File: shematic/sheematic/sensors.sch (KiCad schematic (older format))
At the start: 7 parts

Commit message: cpu updated
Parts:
- IC1: renamed from IC?; symbol bmp180:BMP180 -> sheematic-rescue:BMP180-bmp180
- gave numbers to parts that had none: 6
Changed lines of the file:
@@
 $EndDescr
 $Comp
-L Sensor_Pressure:BMP280 U?
+L Sensor_Pressure:BMP280 U2
 U 1 1 60297DD8
 P 3800 2000
-F 0 "U?" H 4030 2096 50  0000 L CNN
+F 0 "U2" H 4030 2096 50  0000 L CNN
 F 1 "BMP280" H 4030 2005 50  0000 L CNN
 F 2 "Package_LGA:Bosch_LGA-8_2x2.5mm_P0.65mm_ClockwisePinNumbering" H 3800 1300 50  0001 C CNN
@@
 $EndComp
 $Comp
-L Sensor_Gas:CCS811 U?
+L Sensor_Gas:CCS811 U3
 U 1 1 60298425
 P 3800 3900
-F 0 "U?" H 3800 4581 50  0000 C CNN
+F 0 "U3" H 3800 4581 50  0000 C CNN
 F 1 "CCS811" H 3800 4490 50  0000 C CNN
 F 2 "Package_LGA:AMS_LGA-10-1EP_2.7x4mm_P0.6mm" H 3800 3300 50  0001 C CNN
@@
 $EndComp
 $Comp
-L Sensor_Humidity:Si7020-A20 U?
+L Sensor_Humidity:Si7020-A20 U4
 U 1 1 60299163
 P 7000 1900
-F 0 "U?" H 7444 1946 50  0000 L CNN
+F 0 "U4" H 7444 1946 50  0000 L CNN
 F 1 "Si7020-A20" H 7444 1855 50  0000 L CNN
 F 2 "Package_DFN_QFN:DFN-6-1EP_3x3mm_P1mm_EP1.5x2.4mm" H 7000 1500 50  0001 C CNN
@@
 $EndComp
 $Comp
-L Sensor_Humidity:ENS210 U?
+L Sensor_Humidity:ENS210 U5
 U 1 1 602998ED
 P 9050 1900
-F 0 "U?" H 9280 1946 50  0000 L CNN
+F 0 "U5" H 9280 1946 50  0000 L CNN
 F 1 "ENS210" H 9280 1855 50  0000 L CNN
 F 2 "Package_DFN_QFN:AMS_QFN-4-1EP_2x2mm_P0.95mm_EP0.7x1.6mm" H 9050 1500 50  0001 C CNN
@@
 $EndComp
 $Comp
-L bmp180:BMP180 IC?
+L sheematic-rescue:BMP180-bmp180 IC?
 U 1 1 60297945
 P 1300 1850
-F 0 "IC?" H 1850 2115 50  0000 C CNN
+AR Path="/60297945" Ref="IC?"  Part="1"
+AR Path="/60296418/60297945" Ref="IC1"  Part="1"
+F 0 "IC1" H 1850 2115 50  0000 C CNN
 F 1 "BMP180" H 1850 2024 50  0000 C CNN
 F 2 "BMP180" H 2250 1950 50  0001 L CNN
@@
 $EndComp
 $Comp
-L power:GND #PWR?
+L power:GND #PWR0101
 U 1 1 6029BE6D
 P 2400 2650
-F 0 "#PWR?" H 2400 2400 50  0001 C CNN
+F 0 "#PWR0101" H 2400 2400 50  0001 C CNN
 F 1 "GND" H 2405 2477 50  0000 C CNN
 F 2 "" H 2400 2650 50  0001 C CNN
@@
 $EndComp
 $Comp
-L power:GND #PWR?
+L power:GND #PWR0102
 U 1 1 6029C3A8
 P 3800 2650
-F 0 "#PWR?" H 3800 2400 50  0001 C CNN
+F 0 "#PWR0102" H 3800 2400 50  0001 C CNN
 F 1 "GND" H 3805 2477 50  0000 C CNN
 F 2 "" H 3800 2650 50  0001 C CNN
@@
 $EndComp
 $Comp
-L power:GND #PWR?
+L power:GND #PWR0103
 U 1 1 6029C50E
 P 3900 2650
-F 0 "#PWR?" H 3900 2400 50  0001 C CNN
+F 0 "#PWR0103" H 3900 2400 50  0001 C CNN
 F 1 "GND" H 3905 2477 50  0000 C CNN
 F 2 "" H 3900 2650 50  0001 C CNN
@@
 $EndComp
 $Comp
-L power:GND #PWR?
+L power:GND #PWR0104
 U 1 1 6029C6CB
 P 3800 4600
-F 0 "#PWR?" H 3800 4350 50  0001 C CNN
+F 0 "#PWR0104" H 3800 4350 50  0001 C CNN
 F 1 "GND" H 3805 4427 50  0000 C CNN
 F 2 "" H 3800 4600 50  0001 C CNN
@@
 $EndComp
 $Comp
-L power:GND #PWR?
+L power:GND #PWR0105
 U 1 1 6029CA3B
 P 7750 2650
-F 0 "#PWR?" H 7750 2400 50  0001 C CNN
+F 0 "#PWR0105" H 7750 2400 50  0001 C CNN
 F 1 "GND" H 7755 2477 50  0000 C CNN
 F 2 "" H 7750 2650 50  0001 C CNN
@@
 	1100 2050 1300 2050
 $Comp
-L power:+3.3V #PWR?
+L power:+3.3V #PWR0106
 U 1 1 6029E802
 P 1050 1500
-F 0 "#PWR?" H 1050 1350 50  0001 C CNN
+F 0 "#PWR0106" H 1050 1350 50  0001 C CNN
 F 1 "+3.3V" H 1065 1673 50  0000 C CNN
 F 2 "" H 1050 1500 50  0001 C CNN
@@
 Connection ~ 1100 1950
 $Comp
-L power:+3.3V #PWR?
+L power:+3.3V #PWR0107
 U 1 1 6029EF9E
 P 3800 1300
-F 0 "#PWR?" H 3800 1150 50  0001 C CNN
+F 0 "#PWR0107" H 3800 1150 50  0001 C CNN
 F 1 "+3.3V" H 3815 1473 50  0000 C CNN
 F 2 "" H 3800 1300 50  0001 C CNN
@@
 	9150 1200 9150 1600
 $Comp
-L power:+3.3V #PWR?
+L power:+3.3V #PWR0108
 U 1 1 602A1788
 P 8550 1050
-F 0 "#PWR?" H 8550 900 50  0001 C CNN
+F 0 "#PWR0108" H 8550 900 50  0001 C CNN
 F 1 "+3.3V" H 8565 1223 50  0000 C CNN
 F 2 "" H 8550 1050 50  0001 C CNN
@@
 SDA
 $Comp
-L Device:R R?
+L Device:R R1
 U 1 1 602A736D
 P 5250 1150
-F 0 "R?" H 5320 1196 50  0000 L CNN
+F 0 "R1" H 5320 1196 50  0000 L CNN
 F 1 "R" H 5320 1105 50  0000 L CNN
 F 2 "" V 5180 1150 50  0001 C CNN
@@
 $EndComp
 $Comp
-L Device:R R?
+L Device:R R2
 U 1 1 602A7929
 P 5550 1150
-F 0 "R?" H 5620 1196 50  0000 L CNN
+F 0 "R2" H 5620 1196 50  0000 L CNN
 F 1 "R" H 5620 1105 50  0000 L CNN
 F 2 "" V 5480 1150 50  0001 C CNN
@@
 SDA
 $Comp
-L power:+3.3V #PWR?
+L power:+3.3V #PWR0109
 U 1 1 602A8243
 P 5250 800
-F 0 "#PWR?" H 5250 650 50  0001 C CNN
+F 0 "#PWR0109" H 5250 650 50  0001 C CNN
 F 1 "+3.3V" H 5265 973 50  0000 C CNN
 F 2 "" H 5250 800 50  0001 C CNN
@@
 $EndComp
 $Comp
-L power:+3.3V #PWR?
+L power:+3.3V #PWR0110
 U 1 1 602A872F
 P 5550 800
-F 0 "#PWR?" H 5550 650 50  0001 C CNN
+F 0 "#PWR0110" H 5550 650 50  0001 C CNN
 F 1 "+3.3V" H 5565 973 50  0000 C CNN
 F 2 "" H 5550 800 50  0001 C CNN

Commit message: updated
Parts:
- removed IC1: BMP180, BMP180, symbol sheematic-rescue:BMP180-bmp180
- added IC1: BMP180, Sensor:BMP180, symbol SamacSys_Parts:BMP180
- added R3, R4, R5, R6, R7: R, symbol Device:R
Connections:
- net +3V3: now also U3.6 (VDD), IC1.2 (VDD), IC1.3 (VDDIO), R3.1, R5.1, R6.1, R7.1
- net GND: now also U3.11 (GND), IC1.7 (GND), R4.1
- net SCL: now also U3.10 (SCL), IC1.5 (SCL)
- net SDA: now also U3.9 (SDA), IC1.6 (SDA)
- net at U3.1 (ADDR): now also R3.2, R4.2
- net CCS811_nRESET: now reaches U3.2 (~RESET)
- net CCS811_nRESET: now also R6.2
- net CCS811_nINT: now reaches U3.3 (~INT)
- net CCS811_nINT: now also R5.2
- net at U3.4 (PWM): now also U3.5 (Sense)
- net CCS811_nWAKE: now reaches U3.7 (~WAKE)
- net CCS811_nWAKE: now also R7.2

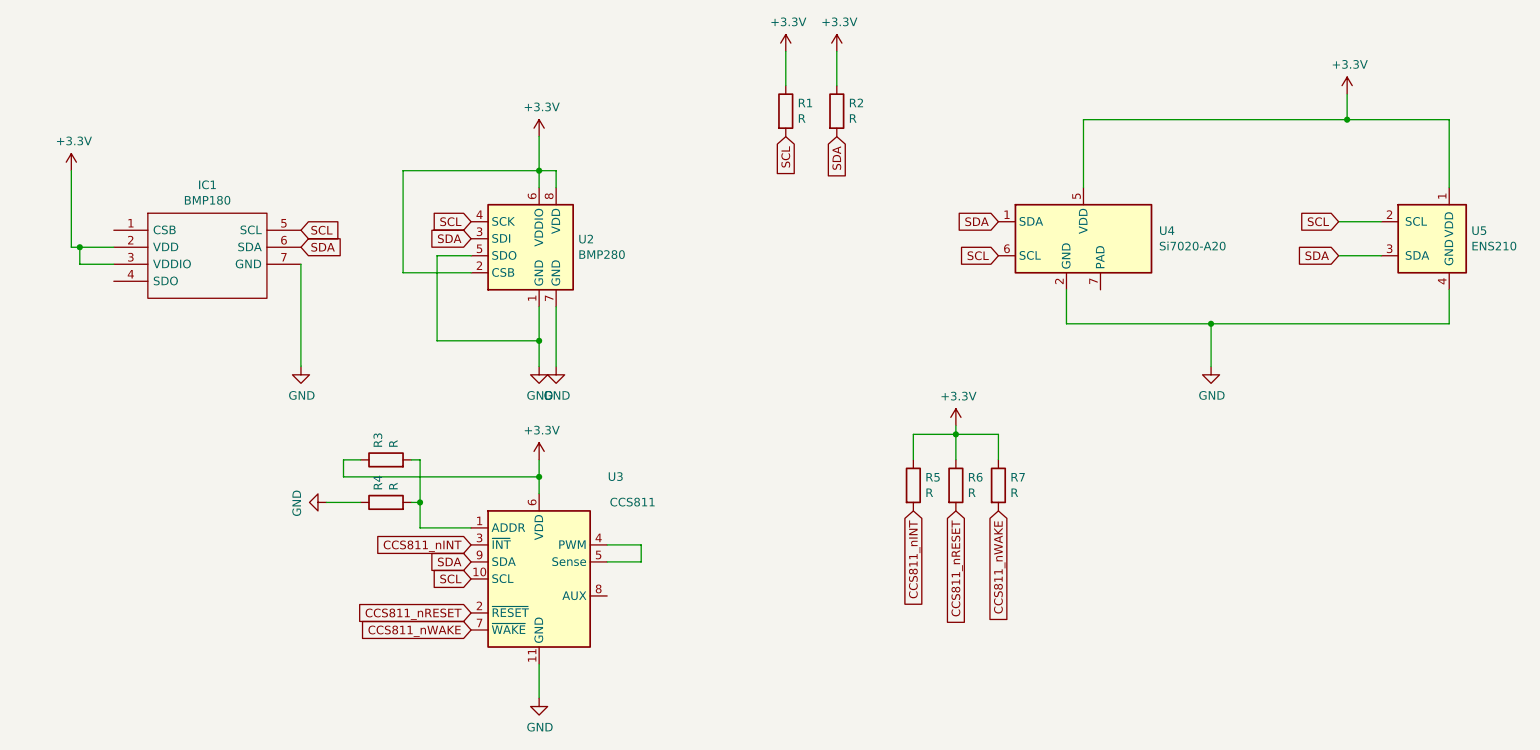
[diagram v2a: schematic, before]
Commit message: modify for warios drive
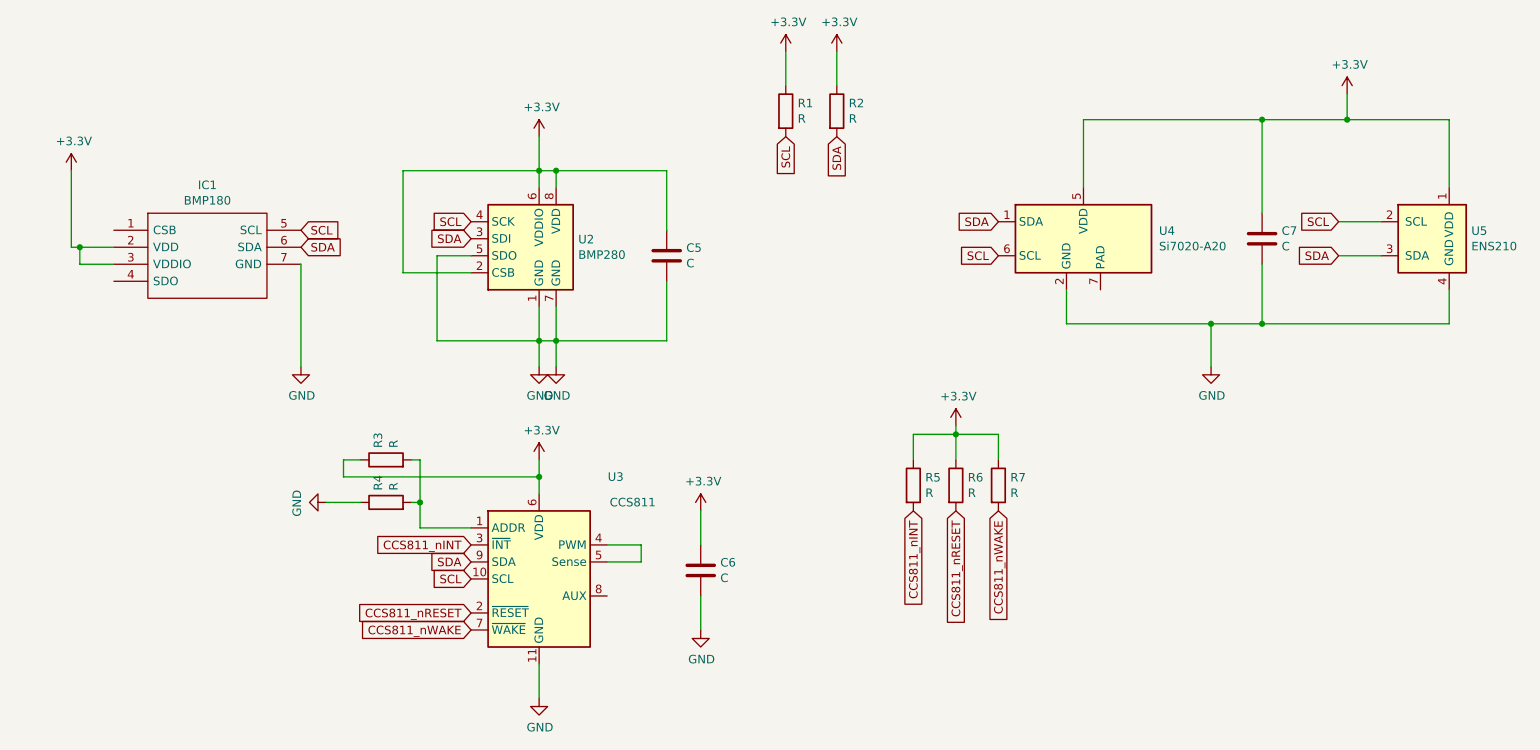
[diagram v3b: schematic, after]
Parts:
- added C5, C6, C7: C, Capacitor_SMD:C_0603_1608Metric_Pad1.08x0.95mm_HandSolder, symbol Device:C
- R1, R2, R3, R4, R5, R6, R7: footprint (none) -> Resistor_SMD:R_0603_1608Metric_Pad1.05x0.95mm_HandSolder
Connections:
- net +3V3: now also C5.1, C6.1, C7.1
- net GND: now also C5.2, C6.2, C7.2
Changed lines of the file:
@@
 	3800 2300 3800 2500
 Wire Wire Line
-	3900 2650 3900 2300
+	3900 2650 3900 2500
 Wire Wire Line
 	2400 2650 2400 2050
@@
 	9150 2200 9150 2400
 Wire Wire Line
-	9150 2400 7750 2400
+	9150 2400 8050 2400
 Connection ~ 7750 2400
 Wire Wire Line
@@
 	7000 1200 7000 1600
 Wire Wire Line
-	7000 1200 8550 1200
+	7000 1200 8050 1200
 Wire Wire Line
 	6900 2200 6900 2400
@@
 F 0 "R1" H 5320 1196 50  0000 L CNN
 F 1 "R" H 5320 1105 50  0000 L CNN
-F 2 "" V 5180 1150 50  0001 C CNN
+F 2 "Resistor_SMD:R_0603_1608Metric_Pad1.05x0.95mm_HandSolder" V 5180 1150 50  0001 C CNN
 F 3 "~" H 5250 1150 50  0001 C CNN
 	1    5250 1150
@@
 F 0 "R2" H 5620 1196 50  0000 L CNN
 F 1 "R" H 5620 1105 50  0000 L CNN
-F 2 "" V 5480 1150 50  0001 C CNN
+F 2 "Resistor_SMD:R_0603_1608Metric_Pad1.05x0.95mm_HandSolder" V 5480 1150 50  0001 C CNN
 F 3 "~" H 5550 1150 50  0001 C CNN
 	1    5550 1150
@@
 F 0 "R3" H 2970 3246 50  0000 L CNN
 F 1 "R" H 2970 3155 50  0000 L CNN
-F 2 "" V 2830 3200 50  0001 C CNN
+F 2 "Resistor_SMD:R_0603_1608Metric_Pad1.05x0.95mm_HandSolder" V 2830 3200 50  0001 C CNN
 F 3 "~" H 2900 3200 50  0001 C CNN
 	1    2900 3200
@@
 F 0 "R4" H 2970 3496 50  0000 L CNN
 F 1 "R" H 2970 3405 50  0000 L CNN
-F 2 "" V 2830 3450 50  0001 C CNN
+F 2 "Resistor_SMD:R_0603_1608Metric_Pad1.05x0.95mm_HandSolder" V 2830 3450 50  0001 C CNN
 F 3 "~" H 2900 3450 50  0001 C CNN
 	1    2900 3450
@@
 F 0 "R5" H 6070 3396 50  0000 L CNN
 F 1 "R" H 6070 3305 50  0000 L CNN
-F 2 "" V 5930 3350 50  0001 C CNN
+F 2 "Resistor_SMD:R_0603_1608Metric_Pad1.05x0.95mm_HandSolder" V 5930 3350 50  0001 C CNN
 F 3 "~" H 6000 3350 50  0001 C CNN
 	1    6000 3350
@@
 F 0 "R6" H 6320 3396 50  0000 L CNN
 F 1 "R" H 6320 3305 50  0000 L CNN
-F 2 "" V 6180 3350 50  0001 C CNN
+F 2 "Resistor_SMD:R_0603_1608Metric_Pad1.05x0.95mm_HandSolder" V 6180 3350 50  0001 C CNN
 F 3 "~" H 6250 3350 50  0001 C CNN
 	1    6250 3350
@@
 F 0 "R7" H 6570 3396 50  0000 L CNN
 F 1 "R" H 6570 3305 50  0000 L CNN
-F 2 "" V 6430 3350 50  0001 C CNN
+F 2 "Resistor_SMD:R_0603_1608Metric_Pad1.05x0.95mm_HandSolder" V 6430 3350 50  0001 C CNN
 F 3 "~" H 6500 3350 50  0001 C CNN
 	1    6500 3350
@@
 	1    0    0    -1
 $EndComp
+$Comp
+L Device:C C6
+U 1 1 602B0CC2
+P 4750 3850
+F 0 "C6" H 4865 3896 50  0000 L CNN
+F 1 "C" H 4865 3805 50  0000 L CNN
+F 2 "Capacitor_SMD:C_0603_1608Metric_Pad1.08x0.95mm_HandSolder" H 4788 3700 50  0001 C CNN
+F 3 "~" H 4750 3850 50  0001 C CNN
+	1    4750 3850
+	1    0    0    -1
+$EndComp
+$Comp
+L Device:C C5
+U 1 1 602B1405
+P 4550 2000
+F 0 "C5" H 4665 2046 50  0000 L CNN
+F 1 "C" H 4665 1955 50  0000 L CNN
+F 2 "Capacitor_SMD:C_0603_1608Metric_Pad1.08x0.95mm_HandSolder" H 4588 1850 50  0001 C CNN
+F 3 "~" H 4550 2000 50  0001 C CNN
+	1    4550 2000
+	1    0    0    -1
+$EndComp
+$Comp
+L Device:C C7
+U 1 1 602B2070
+P 8050 1900
+F 0 "C7" H 8165 1946 50  0000 L CNN
+F 1 "C" H 8165 1855 50  0000 L CNN
+F 2 "Capacitor_SMD:C_0603_1608Metric_Pad1.08x0.95mm_HandSolder" H 8088 1750 50  0001 C CNN
+F 3 "~" H 8050 1900 50  0001 C CNN
+	1    8050 1900
+	1    0    0    -1
+$EndComp
+Wire Wire Line
+	8050 2050 8050 2400
+Connection ~ 8050 2400
+Wire Wire Line
+	8050 2400 7750 2400
+Wire Wire Line
+	8050 1750 8050 1200
+Connection ~ 8050 1200
+Wire Wire Line
+	8050 1200 8550 1200
+$Comp
+L power:+3.3V #PWR0115
+U 1 1 602B463E
+P 4750 3500
+F 0 "#PWR0115" H 4750 3350 50  0001 C CNN
+F 1 "+3.3V" H 4765 3673 50  0000 C CNN
+F 2 "" H 4750 3500 50  0001 C CNN
+F 3 "" H 4750 3500 50  0001 C CNN
+	1    4750 3500
+	1    0    0    -1
+$EndComp
+$Comp
+L power:GND #PWR0116
+U 1 1 602B4C1A
+P 4750 4200
+F 0 "#PWR0116" H 4750 3950 50  0001 C CNN
+F 1 "GND" H 4755 4027 50  0000 C CNN
+F 2 "" H 4750 4200 50  0001 C CNN
+F 3 "" H 4750 4200 50  0001 C CNN
+	1    4750 4200
+	1    0    0    -1
+$EndComp
+Wire Wire Line
+	4750 3700 4750 3500
+Wire Wire Line
+	4750 4200 4750 4000
+Wire Wire Line
+	4550 2150 4550 2500
+Wire Wire Line
+	4550 2500 3900 2500
+Connection ~ 3900 2500
+Wire Wire Line
+	3900 2500 3900 2300
+Wire Wire Line
+	3900 2500 3800 2500
+Wire Wire Line
+	4550 1850 4550 1500
+Wire Wire Line
+	4550 1500 3900 1500
+Connection ~ 3900 1500
 $EndSCHEMATC
